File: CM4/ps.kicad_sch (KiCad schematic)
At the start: 33 parts, among them J1 USB_B, J2 Conn_01x02, J3 Conn_01x02, U3 BQ25887RGET, U4 MAX17643

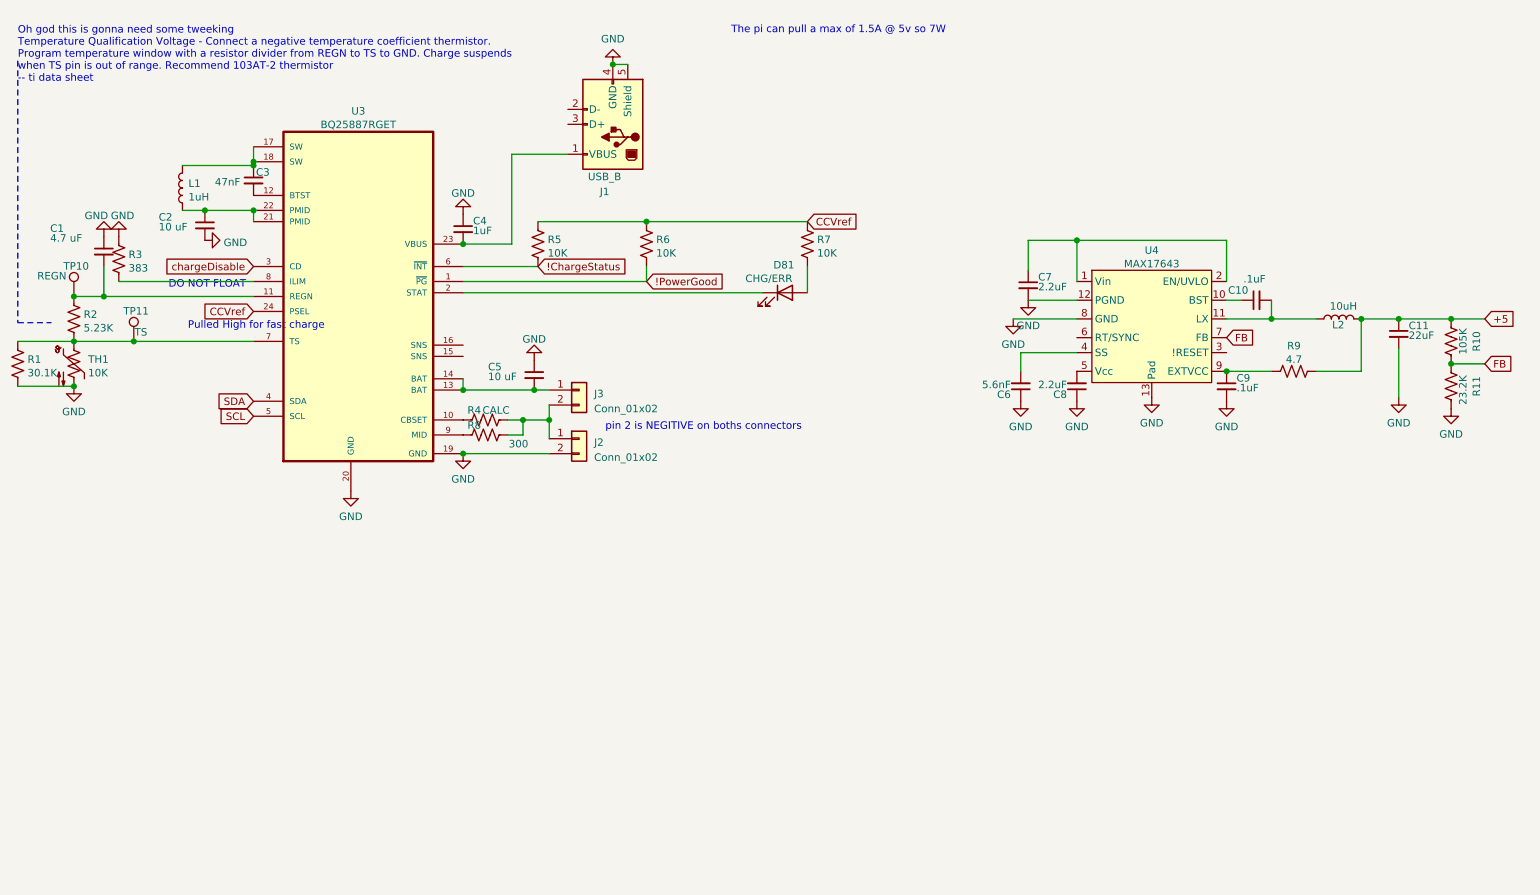
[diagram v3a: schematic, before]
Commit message: Added Power Button Control Circuit
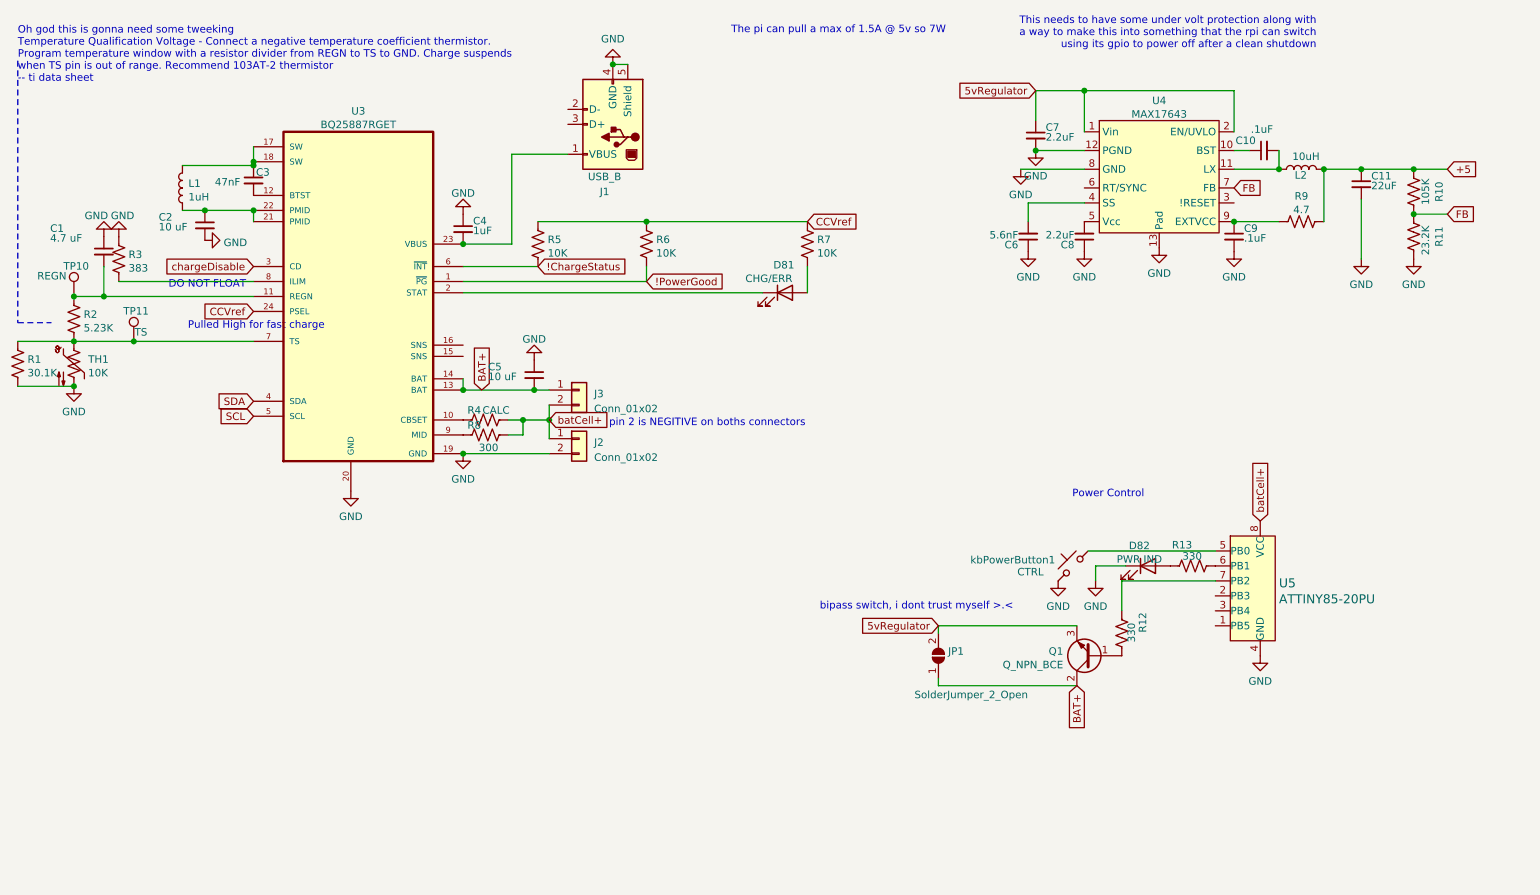
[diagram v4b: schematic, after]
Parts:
- added D82: PWR IND, LED_SMD:LED_2010_5025Metric, symbol Device:LED
- added JP1: SolderJumper_2_Open, Jumper:SolderJumper-2_P1.3mm_Open_RoundedPad1.0x1.5mm, symbol Jumper:SolderJumper_2_Open
- added Q1: Q_NPN_BCE, Package_TO_SOT_SMD:SOT-23, symbol Device:Q_NPN_BCE
- added R12, R13: 330, Resistor_SMD:R_1206_3216Metric, symbol Device:R_US
- added U5: ATTINY85-20PU, digikey-footprints:DIP-8_W7.62mm, symbol dk_Embedded-Microcontrollers:ATTINY85-20PU
- added kbPowerButton1: CTRL, Button_Switch_SMD:SW_SPST_B3SL-1002P, symbol kb5-rescue:SW_Push_45deg-sw_push_45deg-ESP32-S2-WROOM-rescue
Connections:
- net GND: now also D82.1 (K), U5.4 (GND), kbPowerButton1.2
- net batCell+: now reaches J2.1 (Pin_1), J3.2 (Pin_2), R4.1, R8.1
- net batCell+: now also U5.8 (VCC)
- net 5vRegulator: now reaches C7.1, U4.1 (Vin), U4.2 (EN/UVLO)
- net 5vRegulator: now also JP1.2 (B), Q1.3 (E)
- net BAT+: now reaches C5.2, J3.1 (Pin_1), U3.13 (BAT), U3.14 (BAT)
- net BAT+: now also JP1.1 (A), Q1.2 (C)
- new net: U5.5 (PB0), kbPowerButton1.1
- new net: D82.2 (A), R13.2
- new net: R13.1, U5.6 (PB1)
- new net: R12.2, U5.7 (PB2)
- new net: Q1.1 (B), R12.1
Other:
- note added: "Power Control"
- note added: "This needs to have some under volt protection along with a way to make this into something that the rpi can switch using its gpio to power off after a clean shutdown"
- note added: "bipass switch, i dont trust myself >.<"
- moved on the sheet: C10, C11, C6, C7, C8, C9, L2, R10, R11, R9, U4

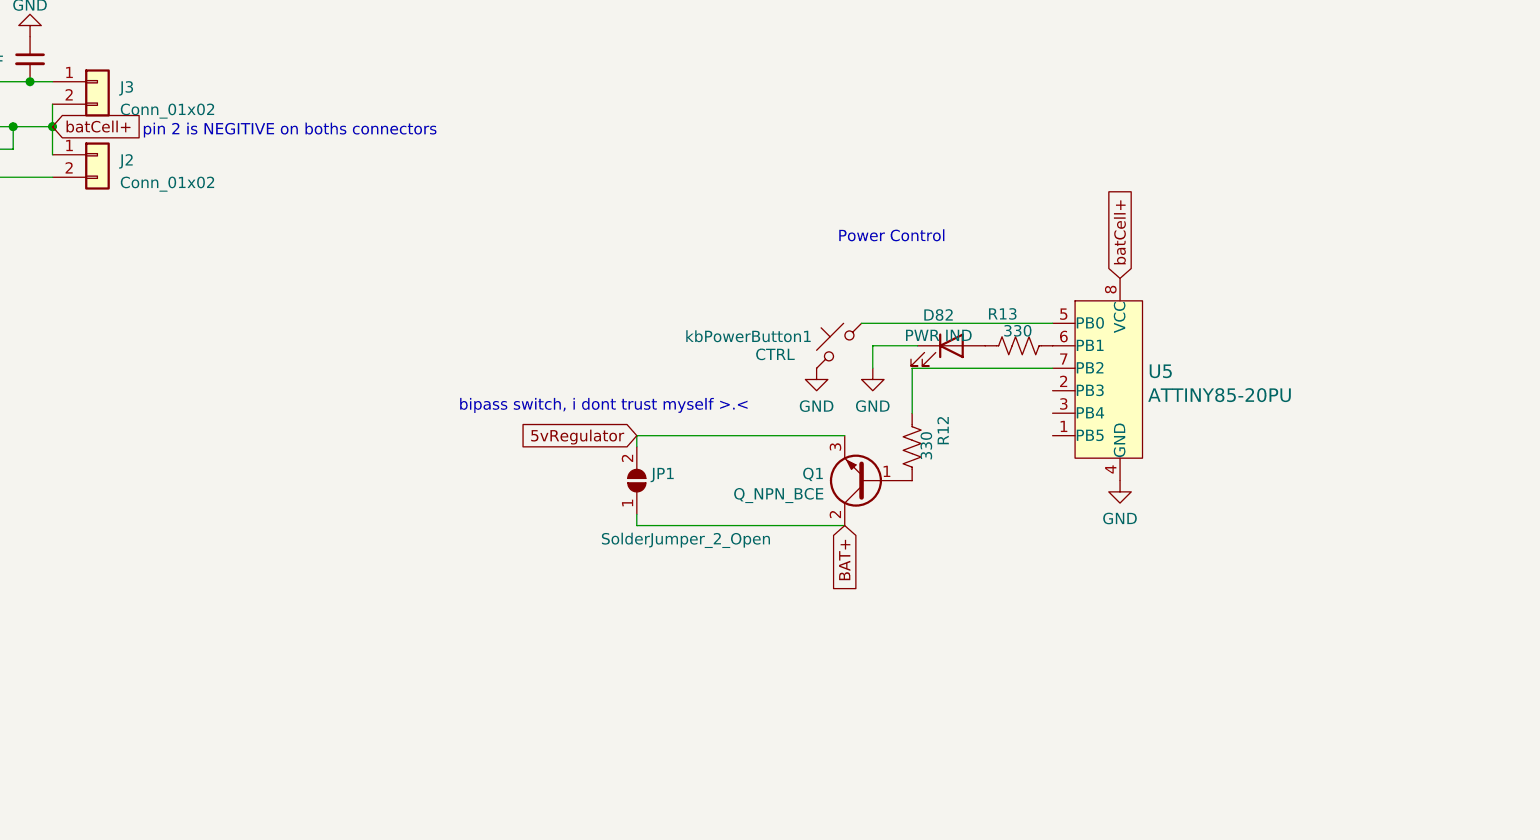
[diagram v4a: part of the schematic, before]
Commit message: Added Power Control Relay
also cleaned up some junk and jank
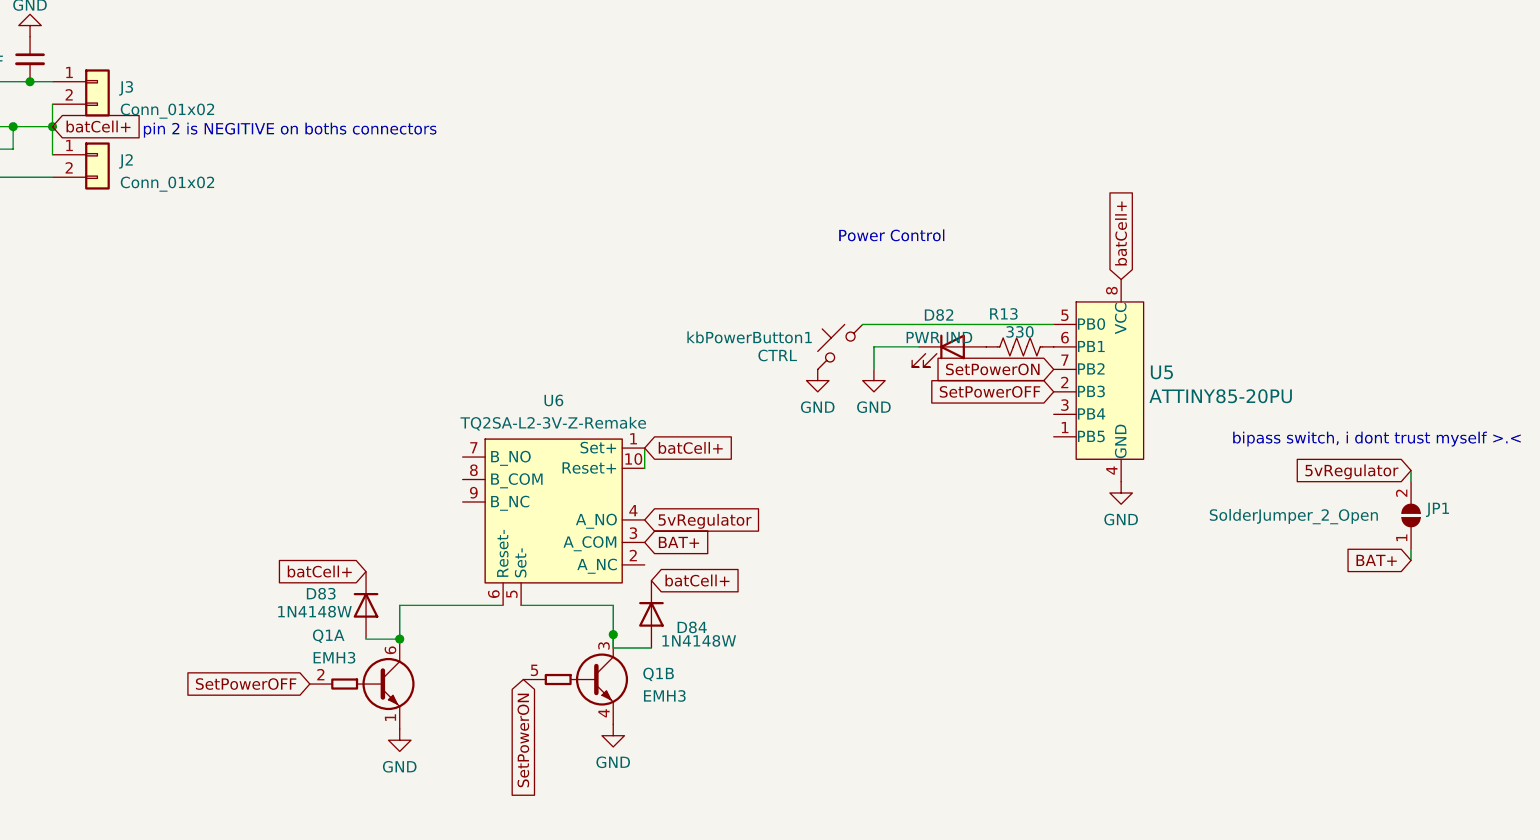
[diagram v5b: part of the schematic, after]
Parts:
- removed Q1: Q_NPN_BCE, Package_TO_SOT_SMD:SOT-23, symbol Device:Q_NPN_BCE
- removed R12: 330, Resistor_SMD:R_1206_3216Metric, symbol Device:R_US
- added D83, D84: 1N4148W, Diode_SMD:D_SOD-123, symbol Diode:1N4148W
- added Q1: EMH3, Package_TO_SOT_SMD:SOT-563, symbol Transistor_BJT:EMH3
- added U6: TQ2SA-L2-3V-Z-Remake, teensy:TQ2SA-L2-3V-Z, symbol Relay:TQ2SA-L2-3V-Z-Remake
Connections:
- net 5vRegulator: now also U6.4 (A_NO)
- net BAT+: now also U6.3 (A_COM)
- net GND: now also Q1.1 (E1), Q1.4 (E2)
- net batCell+: now also D83.1 (K), D84.1 (K), U6.1 (Set+), U6.10 (Reset+)
- net SetPowerOFF: now reaches U5.2 (PB3)
- net SetPowerOFF: now also Q1.2 (B1)
- net SetPowerON: now reaches U5.7 (PB2)
- net SetPowerON: now also Q1.5 (B2)
- new net: D84.2 (A), Q1.3 (C2), U6.5 (Set-)
- new net: D83.2 (A), Q1.6 (C1), U6.6 (Reset-)
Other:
- moved on the sheet: JP1

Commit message: Wrote program discription
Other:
- note added: "pin 2 is NEGITIVE on boths connectors Also should add some sort of lv cut off for batCell+"
- note removed: "pin 2 is NEGITIVE on boths connectors"
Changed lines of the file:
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@@
     (effects (font (size 1.27 1.27)) (justify right bottom))
   )
-  (text "pin 2 is NEGITIVE on boths connectors" (at 114.935 87.63 0)
+  (text "pin 2 is NEGITIVE on boths connectors\nAlso should add some sort of lv cut off\nfor batCell+"
+    (at 121.539 91.694 0)
     (effects (font (size 1.27 1.27)) (justify left bottom))
   )

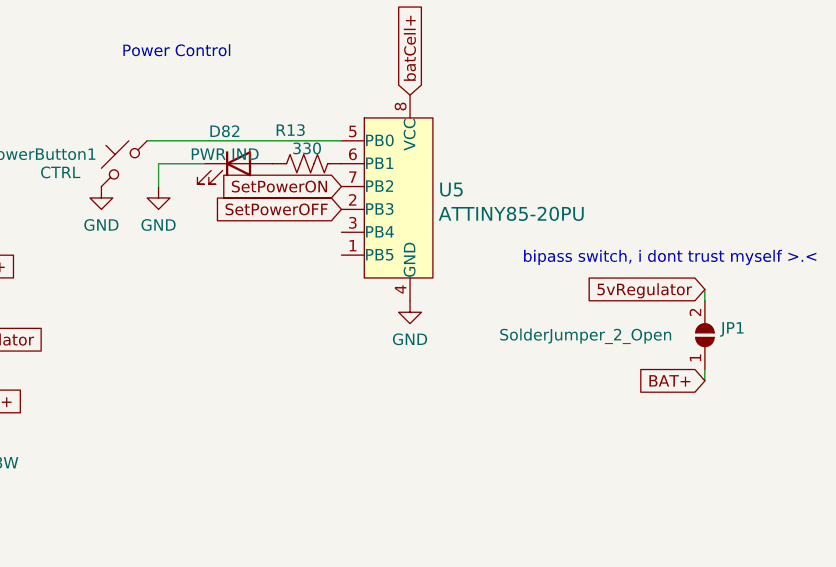
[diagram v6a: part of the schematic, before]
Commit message: Removed Keyboard Matrix Diodes and Added PowerLED and ActivityLED
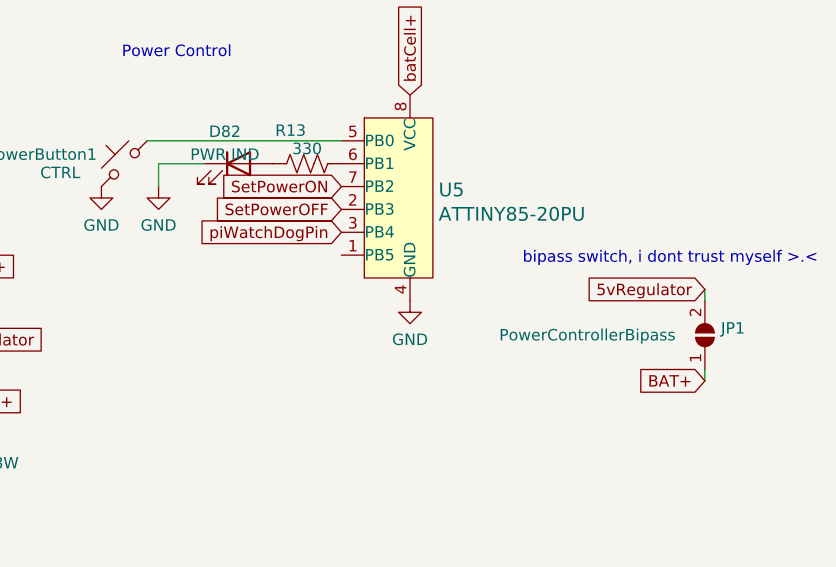
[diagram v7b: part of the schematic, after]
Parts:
- JP1: value SolderJumper_2_Open -> PowerControllerBipass
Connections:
- net piWatchDogPin: now reaches U5.3 (PB4)
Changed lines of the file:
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@@
+    )
+  )
+  (global_label "piWatchDogPin" (shape input) (at 217.932 118.872 180)
+    (effects (font (size 1.27 1.27)) (justify right))
+    (property "Intersheet References" "${INTERSHEET_REFS}" (id 0) (at 201.6094 118.7926 0)
+      (effects (font (size 1.27 1.27)) (justify right) hide)
     )
   )
@@
       (effects (font (size 1.27 1.27)) (justify right))
     )
-    (property "Value" "SolderJumper_2_Open" (id 1) (at 235.458 130.302 90)
-      (effects (font (size 1.27 1.27)) (justify right))
-    )
+    (property "Value" "PowerControllerBipass" (id 1) (at 235.458 130.302 90)
+      (effects (font (size 1.27 1.27)) (justify right))
+    )
